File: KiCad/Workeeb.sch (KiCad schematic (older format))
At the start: 100 parts

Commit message: Add some backup files and more MX labels
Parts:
- MX1, MX10, MX101, MX102, MX103, MX12, MX13, MX14, MX15, MX17, MX18, MX19, MX2, MX20, MX21, MX23, MX24, MX25, MX26, MX28, MX29, MX30, MX32, MX33, MX34, MX35, MX36, MX38, MX39, MX4, MX40, MX41, MX43, MX44, MX45, MX46, MX48, MX49, MX5, MX50, MX51, MX53, MX54, MX55, MX56, MX57, MX59, MX6, MX60, MX61, MX62, MX63, MX65, MX66, MX67, MX69, MX7, MX70, MX71, MX72, MX73, MX75, MX76, MX77, MX78, MX79, MX8, MX80, MX81, MX82, MX83, MX84, MX85, MX86, MX87, MX89, MX9, MX90, MX91, MX92, MX93, MX95, MX96, MX97, MX98, MX99: symbol MX_Alps_Hybrid:MX-NoLED -> Workeeb-rescue:MX-NoLED-MX_Alps_Hybrid
- MX11: value MX-NoLED -> Q; symbol MX_Alps_Hybrid:MX-NoLED -> Workeeb-rescue:MX-NoLED-MX_Alps_Hybrid
- MX16: value MX-NoLED -> W; symbol MX_Alps_Hybrid:MX-NoLED -> Workeeb-rescue:MX-NoLED-MX_Alps_Hybrid
- MX22: value MX-NoLED -> E; symbol MX_Alps_Hybrid:MX-NoLED -> Workeeb-rescue:MX-NoLED-MX_Alps_Hybrid
- MX27: value MX-NoLED -> R; symbol MX_Alps_Hybrid:MX-NoLED -> Workeeb-rescue:MX-NoLED-MX_Alps_Hybrid
- MX3: value MX-NoLED -> Tab; symbol MX_Alps_Hybrid:MX-NoLED -> Workeeb-rescue:MX-NoLED-MX_Alps_Hybrid
- MX31: value MX-NoLED -> T; symbol MX_Alps_Hybrid:MX-NoLED -> Workeeb-rescue:MX-NoLED-MX_Alps_Hybrid
- MX37: value MX-NoLED -> Y; symbol MX_Alps_Hybrid:MX-NoLED -> Workeeb-rescue:MX-NoLED-MX_Alps_Hybrid
- MX42: value MX-NoLED -> U; symbol MX_Alps_Hybrid:MX-NoLED -> Workeeb-rescue:MX-NoLED-MX_Alps_Hybrid
- MX47: value MX-NoLED -> I; symbol MX_Alps_Hybrid:MX-NoLED -> Workeeb-rescue:MX-NoLED-MX_Alps_Hybrid
- MX52: value MX-NoLED -> O; symbol MX_Alps_Hybrid:MX-NoLED -> Workeeb-rescue:MX-NoLED-MX_Alps_Hybrid
- MX58: value MX-NoLED -> P; symbol MX_Alps_Hybrid:MX-NoLED -> Workeeb-rescue:MX-NoLED-MX_Alps_Hybrid
- MX64: value MX-NoLED -> [; symbol MX_Alps_Hybrid:MX-NoLED -> Workeeb-rescue:MX-NoLED-MX_Alps_Hybrid
- MX68: value MX-NoLED -> ]; symbol MX_Alps_Hybrid:MX-NoLED -> Workeeb-rescue:MX-NoLED-MX_Alps_Hybrid
- MX74: value MX-NoLED -> \\; symbol MX_Alps_Hybrid:MX-NoLED -> Workeeb-rescue:MX-NoLED-MX_Alps_Hybrid

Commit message: Finish setting values of switches, start PCB placement
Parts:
- removed MX83: Knob, symbol Workeeb-rescue:MX-NoLED-MX_Alps_Hybrid
- added MX83: Knob, Rotary_Encoder:RotaryEncoder_Alps_EC12E-Switch_Vertical_H20mm, symbol Device:Rotary_Encoder_Switch
- MX1, MX10, MX101, MX11, MX14, MX15, MX16, MX2, MX20, MX21, MX22, MX25, MX26, MX27, MX30, MX31, MX35, MX36, MX37, MX40, MX41, MX42, MX45, MX46, MX47, MX50, MX51, MX52, MX56, MX57, MX58, MX6, MX62, MX63, MX64, MX67, MX68, MX72, MX77, MX78, MX84, MX89, MX9, MX95: footprint (none) -> MX_Only:MXOnly-1U-NoLED
- MX102: value MX-NoLED -> +; footprint (none) -> MX_Only:MXOnly-2U-NoLED
- MX103: value MX-NoLED -> Ent; footprint (none) -> MX_Only:MXOnly-2U-NoLED
- MX12: value MX-NoLED -> A; footprint (none) -> MX_Only:MXOnly-1U-NoLED
- MX13: value MX-NoLED -> Z; footprint (none) -> MX_Only:MXOnly-1U-NoLED
- MX17: value MX-NoLED -> S; footprint (none) -> MX_Only:MXOnly-1U-NoLED
- MX18: value MX-NoLED -> X; footprint (none) -> MX_Only:MXOnly-1U-NoLED
- MX19: value MX-NoLED -> Alt; footprint (none) -> MX_Only:MXOnly-1.25U-NoLED
- MX23: value MX-NoLED -> D; footprint (none) -> MX_Only:MXOnly-1U-NoLED
- MX24: value MX-NoLED -> C; footprint (none) -> MX_Only:MXOnly-1U-NoLED
- MX28: value MX-NoLED -> F; footprint (none) -> MX_Only:MXOnly-1U-NoLED
- MX29: value MX-NoLED -> V; footprint (none) -> MX_Only:MXOnly-1U-NoLED
- MX3, MX74: footprint (none) -> MX_Only:MXOnly-1.5U-NoLED
- MX32: value MX-NoLED -> G; footprint (none) -> MX_Only:MXOnly-1U-NoLED
- MX33: value MX-NoLED -> B; footprint (none) -> MX_Only:MXOnly-1U-NoLED
- MX34: value MX-NoLED -> Space; footprint (none) -> MX_Only:MXOnly-6.25U-NoLED
- MX38: value MX-NoLED -> H; footprint (none) -> MX_Only:MXOnly-1U-NoLED
- MX39: value MX-NoLED -> N; footprint (none) -> MX_Only:MXOnly-1U-NoLED
- MX4: value MX-NoLED -> Caps Lock; footprint (none) -> MX_Only:MXOnly-1.75U-NoLED
- MX43: value MX-NoLED -> J; footprint (none) -> MX_Only:MXOnly-1U-NoLED
- MX44: value MX-NoLED -> M; footprint (none) -> MX_Only:MXOnly-1U-NoLED
- MX48: value MX-NoLED -> K; footprint (none) -> MX_Only:MXOnly-1U-NoLED
- MX49: value MX-NoLED -> ,; footprint (none) -> MX_Only:MXOnly-1U-NoLED
- MX5: value MX-NoLED -> Ctrl; footprint (none) -> MX_Only:MXOnly-1.25U-NoLED
- MX53: value MX-NoLED -> L; footprint (none) -> MX_Only:MXOnly-1U-NoLED
- MX54, MX99: value MX-NoLED -> .; footprint (none) -> MX_Only:MXOnly-1U-NoLED
- MX55: value MX-NoLED -> R-Alt; footprint (none) -> MX_Only:MXOnly-1U-NoLED
- MX59: value MX-NoLED -> ;; footprint (none) -> MX_Only:MXOnly-1U-NoLED
- MX60: value MX-NoLED -> /; footprint (none) -> MX_Only:MXOnly-1U-NoLED
- MX61: value MX-NoLED -> Fn; footprint (none) -> MX_Only:MXOnly-1U-NoLED
- MX65: value MX-NoLED -> '; footprint (none) -> MX_Only:MXOnly-1U-NoLED
- MX66: value MX-NoLED -> R-Ctrl; footprint (none) -> MX_Only:MXOnly-1U-NoLED
- MX69: value MX-NoLED -> Enter; footprint (none) -> MX_Only:MXOnly-2.25U-NoLED
- MX7: value MX-NoLED -> Shift; footprint (none) -> MX_Only:MXOnly-2.25U-NoLED
- MX70: value MX-NoLED -> Shift; footprint (none) -> MX_Only:MXOnly-1.75U-NoLED
- MX71: value MX-NoLED -> Left; footprint (none) -> MX_Only:MXOnly-1U-NoLED
- MX73: footprint (none) -> MX_Only:MXOnly-2U-NoLED
- MX75: value MX-NoLED -> Up; footprint (none) -> MX_Only:MXOnly-1U-NoLED
- MX76: value MX-NoLED -> Down; footprint (none) -> MX_Only:MXOnly-1U-NoLED
- MX79: value MX-NoLED -> PgUp; footprint (none) -> MX_Only:MXOnly-1U-NoLED
- MX8: value MX-NoLED -> Win; footprint (none) -> MX_Only:MXOnly-1.25U-NoLED
- MX80: value MX-NoLED -> PgDn; footprint (none) -> MX_Only:MXOnly-1U-NoLED
- MX81: value MX-NoLED -> Delete; footprint (none) -> MX_Only:MXOnly-1U-NoLED
- MX82: value MX-NoLED -> Right; footprint (none) -> MX_Only:MXOnly-1U-NoLED
- MX85: value MX-NoLED -> 7; footprint (none) -> MX_Only:MXOnly-1U-NoLED
- MX86: value MX-NoLED -> 4; footprint (none) -> MX_Only:MXOnly-1U-NoLED
- MX87: value MX-NoLED -> 1; footprint (none) -> MX_Only:MXOnly-1U-NoLED
- MX90: value MX-NoLED -> 8; footprint (none) -> MX_Only:MXOnly-1U-NoLED
- MX91: value MX-NoLED -> 5; footprint (none) -> MX_Only:MXOnly-1U-NoLED
- MX92: value MX-NoLED -> 2; footprint (none) -> MX_Only:MXOnly-1U-NoLED
- MX93: value MX-NoLED -> 0; footprint (none) -> MX_Only:MXOnly-2U-NoLED
- MX96: value MX-NoLED -> 9; footprint (none) -> MX_Only:MXOnly-1U-NoLED
- MX97: value MX-NoLED -> 6; footprint (none) -> MX_Only:MXOnly-1U-NoLED
- MX98: value MX-NoLED -> 3; footprint (none) -> MX_Only:MXOnly-1U-NoLED
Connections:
- wire segments 200 -> 199

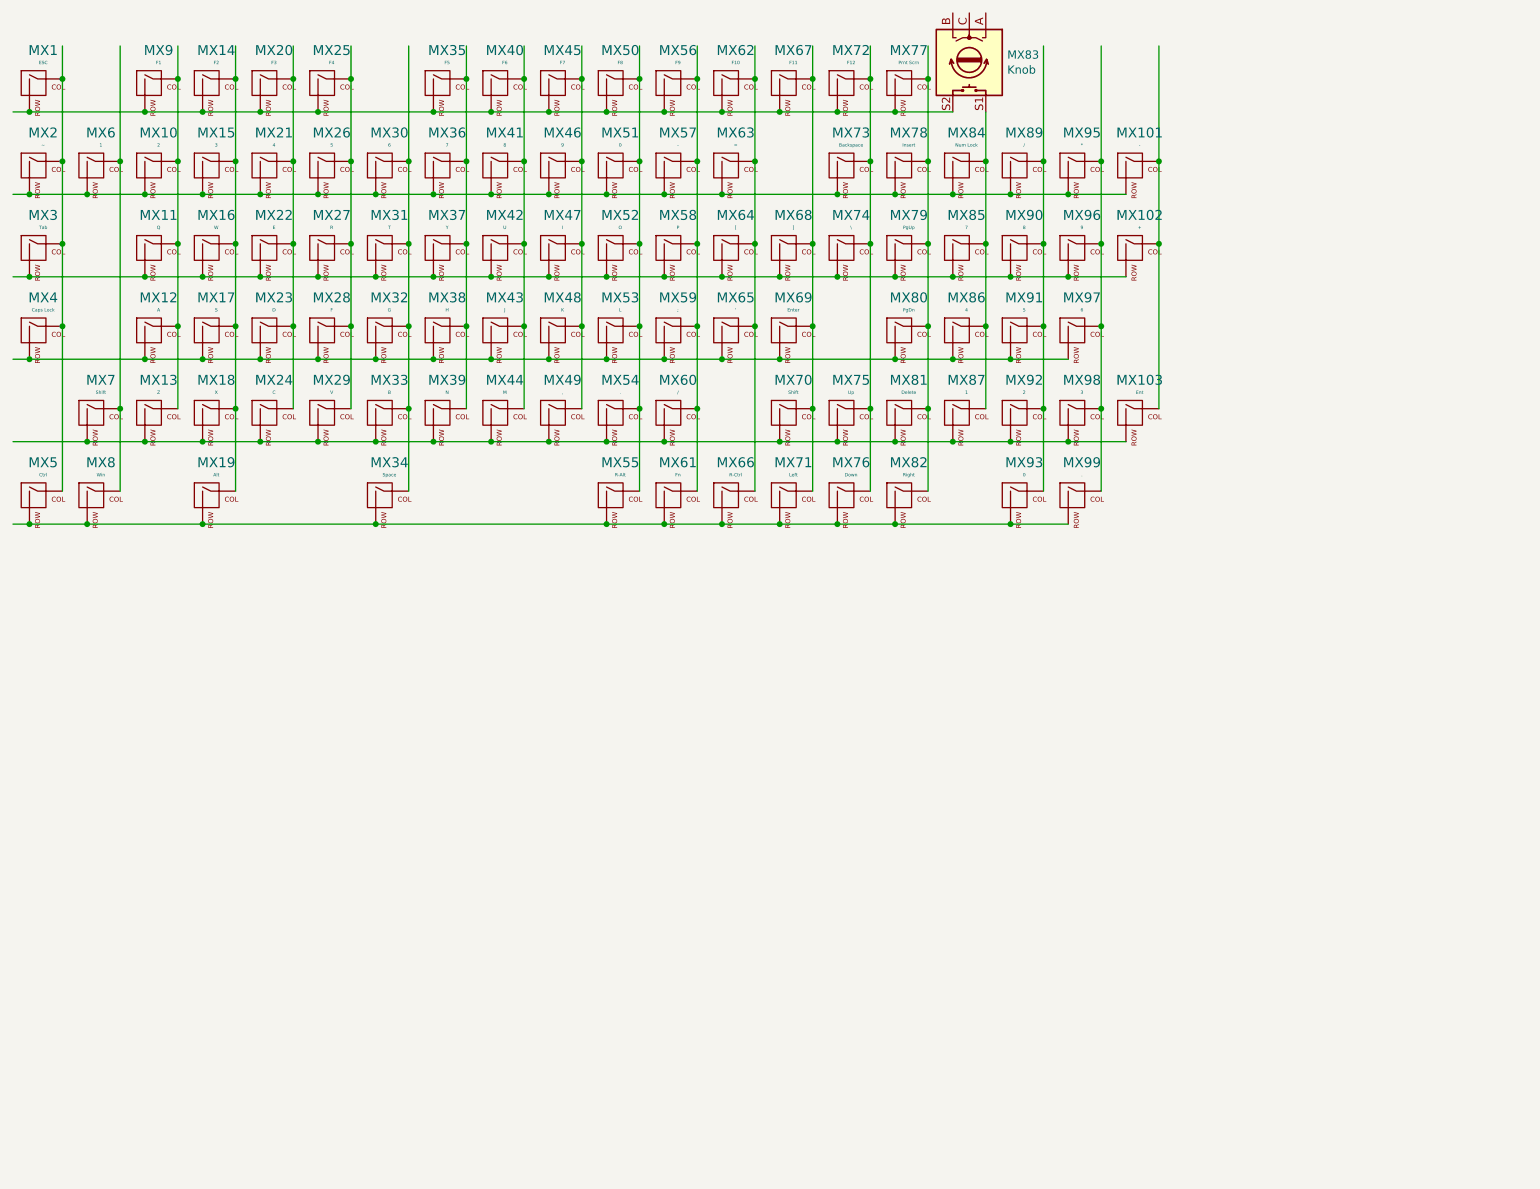
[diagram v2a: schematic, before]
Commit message: Add chosen MCU lib and connect a little
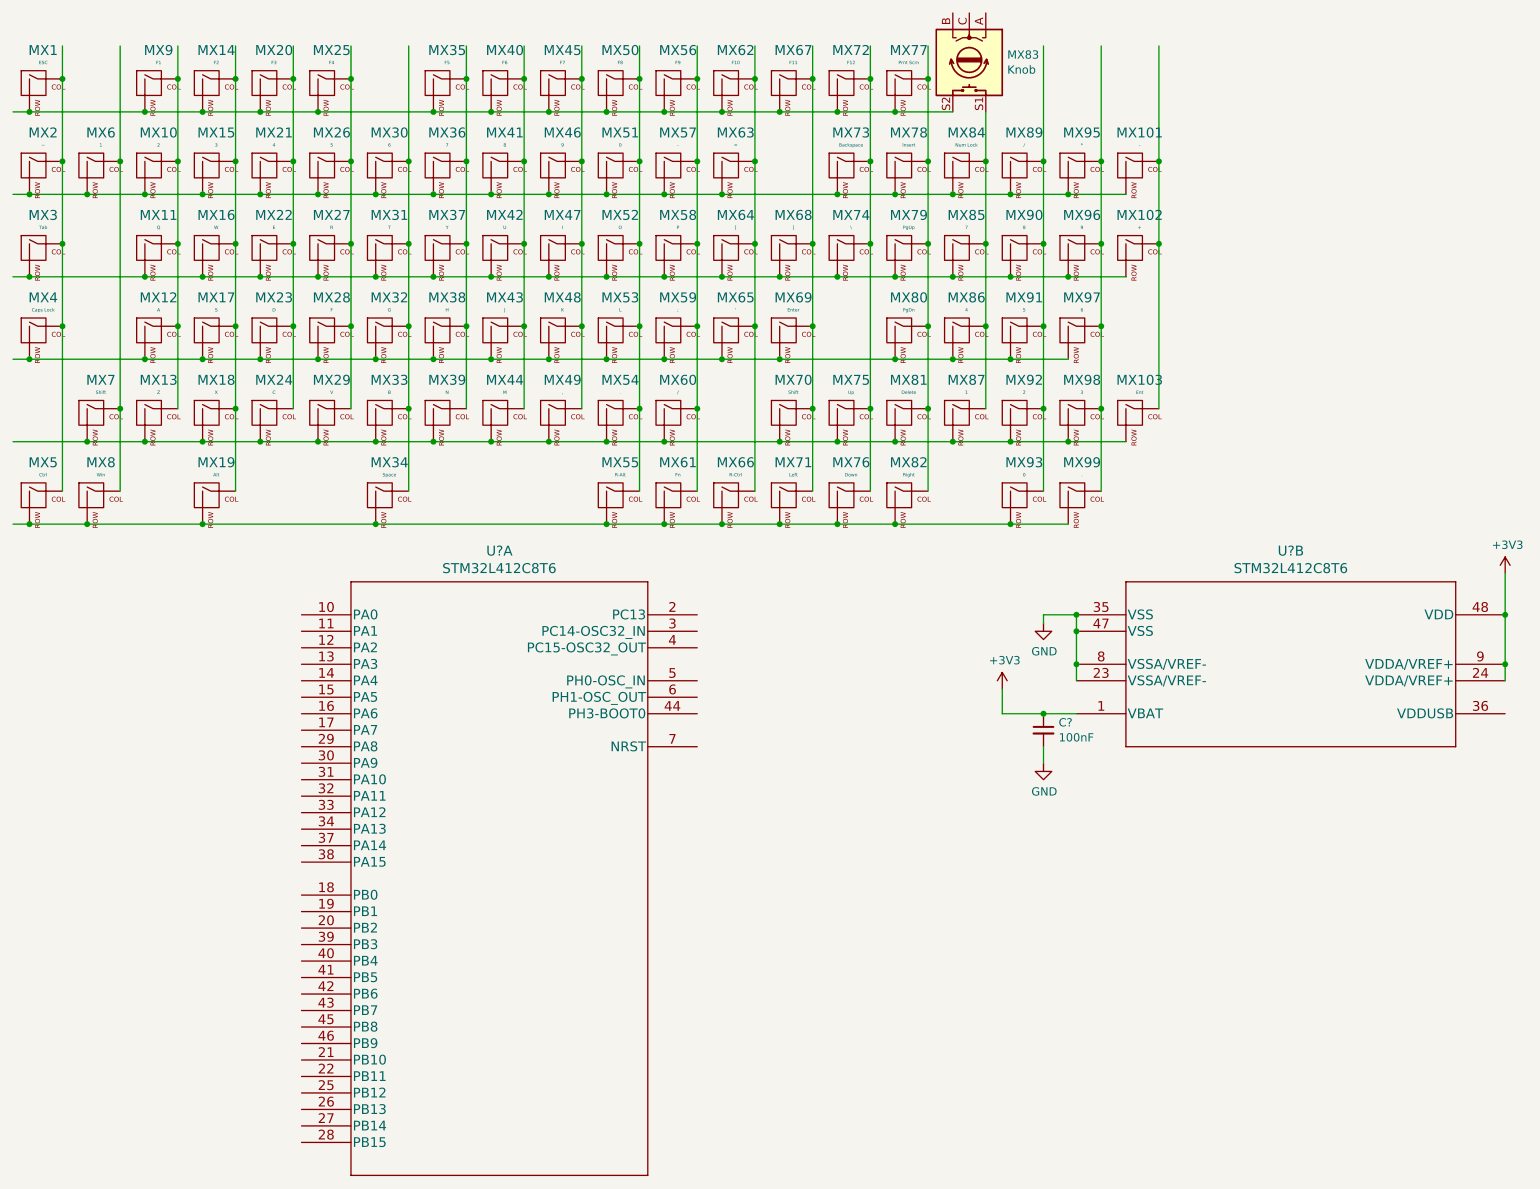
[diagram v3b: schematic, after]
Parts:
- added C?: 100nF, symbol Device:C_Small
- added U? (x2): STM32L412C8T6, LQFP-48, symbol STM32L412C8T6:STM32L412C8T6
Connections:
- net labels added: +3V3, GND
- wire segments 199 -> 211
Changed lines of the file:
@@
 Wire Wire Line
 	6650 1200 6650 1500
+$Comp
+L STM32L412C8T6:STM32L412C8T6 U?
+U 1 1 6202699F
+P 2500 4250
+F 0 "U?" H 3700 4637 60  0000 C CNN
+F 1 "STM32L412C8T6" H 3700 4531 60  0000 C CNN
+F 2 "LQFP-48" H 3700 4490 60  0001 C CNN
+F 3 "" H 2500 4250 60  0000 C CNN
+	1    2500 4250
+	1    0    0    -1
+$EndComp
+$Comp
+L STM32L412C8T6:STM32L412C8T6 U?
+U 2 1 6203009A
+P 7200 4250
+F 0 "U?" H 8500 4637 60  0000 C CNN
+F 1 "STM32L412C8T6" H 8500 4531 60  0000 C CNN
+F 2 "LQFP-48" H 8400 4490 60  0001 C CNN
+F 3 "" H 7200 4250 60  0000 C CNN
+	2    7200 4250
+	1    0    0    -1
+$EndComp
+$Comp
+L Device:C_Small C?
+U 1 1 6203DBCE
+P 7000 4950
+F 0 "C?" H 7092 4996 50  0000 L CNN
+F 1 "100nF" H 7092 4905 50  0000 L CNN
+F 2 "" H 7000 4950 50  0001 C CNN
+F 3 "~" H 7000 4950 50  0001 C CNN
+	1    7000 4950
+	1    0    0    -1
+$EndComp
+Wire Wire Line
+	7200 4850 7000 4850
+Connection ~ 7000 4850
+Wire Wire Line
+	7000 4850 6750 4850
+Wire Wire Line
+	7000 5050 7000 5150
+$Comp
+L power:GND #PWR?
+U 1 1 62054B6D
+P 7000 5150
+F 0 "#PWR?" H 7000 4900 50  0001 C CNN
+F 1 "GND" H 7005 4977 50  0000 C CNN
+F 2 "" H 7000 5150 50  0001 C CNN
+F 3 "" H 7000 5150 50  0001 C CNN
+	1    7000 5150
+	1    0    0    -1
+$EndComp
+$Comp
+L power:+3V3 #PWR?
+U 1 1 62063635
+P 9800 4000
+F 0 "#PWR?" H 9800 3850 50  0001 C CNN
+F 1 "+3V3" H 9815 4173 50  0000 C CNN
+F 2 "" H 9800 4000 50  0001 C CNN
+F 3 "" H 9800 4000 50  0001 C CNN
+	1    9800 4000
+	1    0    0    -1
+$EndComp
+$Comp
+L power:+3V3 #PWR?
+U 1 1 62064F17
+P 6750 4700
+F 0 "#PWR?" H 6750 4550 50  0001 C CNN
+F 1 "+3V3" H 6765 4873 50  0000 C CNN
+F 2 "" H 6750 4700 50  0001 C CNN
+F 3 "" H 6750 4700 50  0001 C CNN
+	1    6750 4700
+	1    0    0    -1
+$EndComp
+Wire Wire Line
+	6750 4850 6750 4700
+Wire Wire Line
+	9800 4650 9800 4550
+Connection ~ 9800 4250
+Connection ~ 9800 4550
+Wire Wire Line
+	9800 4550 9800 4250
+Wire Wire Line
+	9800 4250 9800 4000
+Wire Wire Line
+	7200 4650 7200 4550
+Wire Wire Line
+	7200 4250 7000 4250
+Wire Wire Line
+	7000 4250 7000 4300
+Connection ~ 7200 4250
+Connection ~ 7200 4350
+Wire Wire Line
+	7200 4350 7200 4250
+Connection ~ 7200 4550
+Wire Wire Line
+	7200 4550 7200 4350
+$Comp
+L power:GND #PWR?
+U 1 1 6209EDE2
+P 7000 4300
+F 0 "#PWR?" H 7000 4050 50  0001 C CNN
+F 1 "GND" H 7005 4127 50  0000 C CNN
+F 2 "" H 7000 4300 50  0001 C CNN
+F 3 "" H 7000 4300 50  0001 C CNN
+	1    7000 4300
+	1    0    0    -1
+$EndComp
 $EndSCHEMATC
